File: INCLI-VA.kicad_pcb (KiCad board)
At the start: 2 copper layers, 100 x 100 mm, 168 parts, among them J1 MSTBV 2,5/5-GF-5,08, J2 MSTBV 2,5/2-GF-5,08, J401 USB4105-GF-A, J402 UART0, Q101 STD18NF25, Q102 IPD30N10S3L-34, Q701 DMN10H220LQ, Q751 DMN10H220LQ, SW401 RESET, SW402 BOOT, U101 LM74930QRGERQ1, U201 LMR38010SQDDARQ1, U301 TPS62A02QDRLRQ1, U302 LP5907QMFX-3.3Q1, U401 ESP32-S3-WROOM-1-N8R2, U402 USBLC6-2SC6, U501 SCL3300-D01, U502 ASM330LHHTR, U503 AS5147U-HTSM, U601 ADM3055E, U701 74AHCT1G126, U751 74AHCT1G126, U801 TPS3828-33Q1

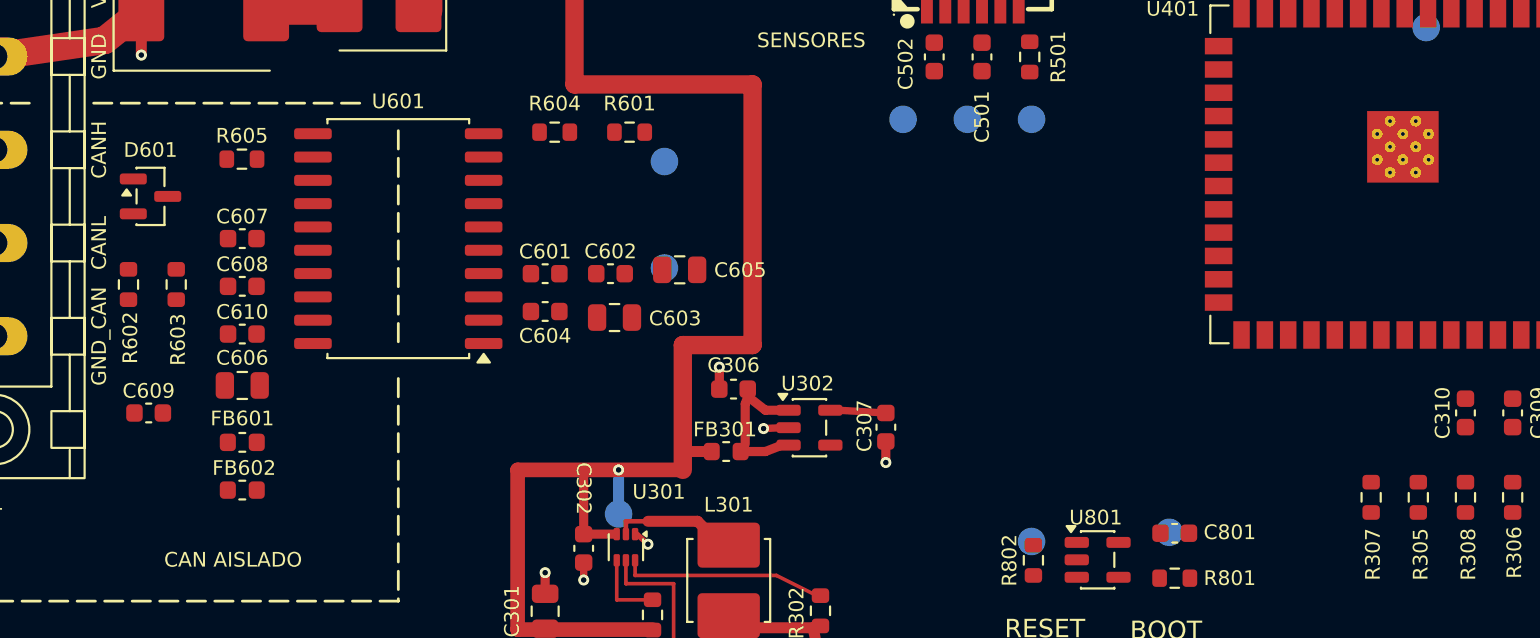
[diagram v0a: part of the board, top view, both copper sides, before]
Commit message: [Codex] ruteo etapa 2 parcial: fuente CAN, desacoples, señales lógicas y TP301
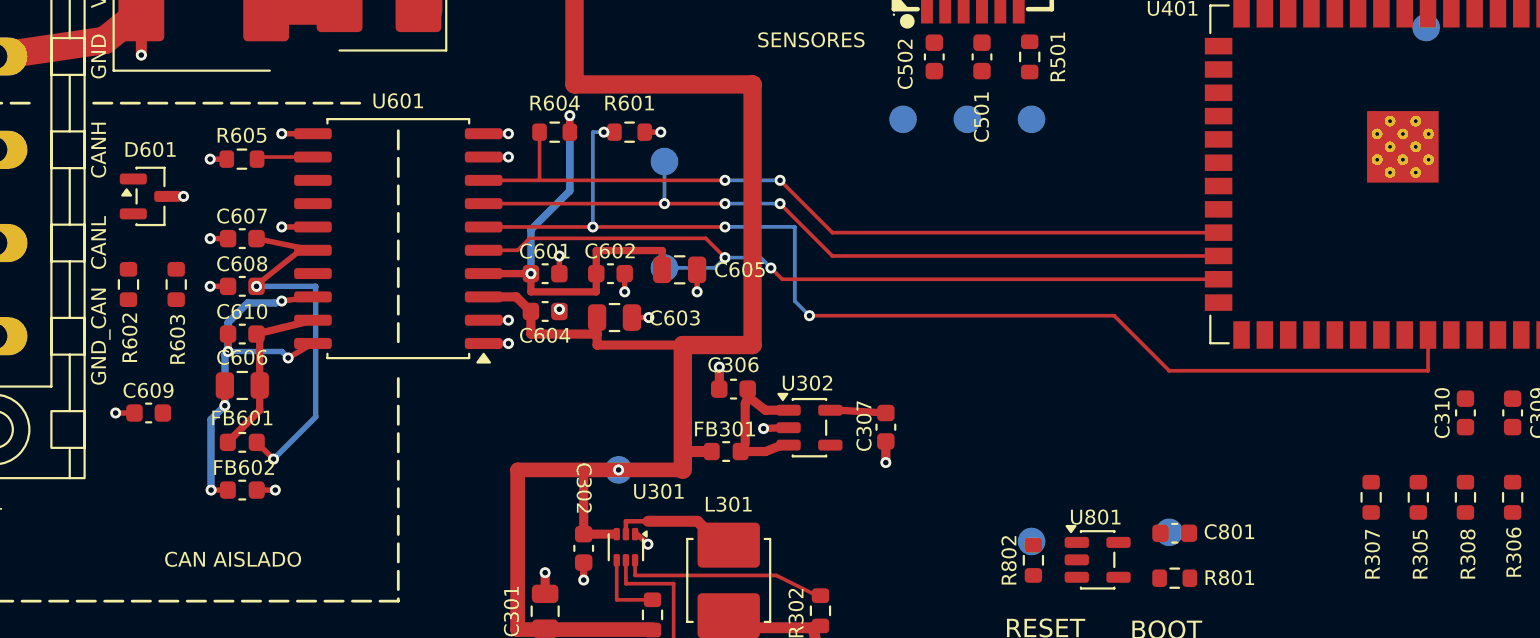
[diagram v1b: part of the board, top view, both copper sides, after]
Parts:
- moved TP301 2.40 mm to (140.0, 131.6)
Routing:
- net /CAN_SILENT: track 0.00 -> 65.3 mm, vias 0 -> 4
- net /CAN_RX: track 0.00 -> 44.8 mm, vias 0 -> 2
- net /CAN_STBY: track 0.00 -> 43.8 mm, vias 0 -> 2
- net /CAN_TX: track 0.00 -> 43.5 mm, vias 0 -> 3
- net +3V3_D: track 15.9 -> 40.3 mm, vias 1 -> 3
- net /60_can/GNDISO_CAN: track 0.00 -> 22.6 mm, vias 0 -> 5
- net /60_can/V_SOIN: track 0.00 -> 21.8 mm, vias 0 -> 2
- net +5V_VEH: track 148.1 -> 159.6 mm
- net GND_VEH: track 40.4 -> 50.8 mm, vias 19 -> 29
- net /60_can/V_SOOUT: track 0.09 -> 9.95 mm
- net GND_CAN: track 0.00 -> 9.15 mm, vias 0 -> 8
- net /60_can/CAN_RS: track 0.16 -> 3.09 mm

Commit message: [Codex] ruteo etapa 2: cierra CAN, terminación y verificación de longitudes
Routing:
- net /BUS_CAN_H: track 0.00 -> 30.8 mm, vias 0 -> 2
- net /BUS_CAN_L: track 0.00 -> 25.0 mm
- net Net-(C609-Pad1): track 0.03 -> 11.6 mm, vias 0 -> 2

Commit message: [Codex] ruteo: audita continuidad CAN y avanza etapa 3 parcial
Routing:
- net +3V3_D: track 40.3 -> 119.0 mm, vias 3 -> 5
- net /MCU_RST_N: track 0.00 -> 62.1 mm, vias 0 -> 2
- net /40_mcu/BOOT: track 0.00 -> 29.2 mm, vias 0 -> 3
- net /40_mcu/U0TXD: track 0.00 -> 24.9 mm, vias 0 -> 2
- net /40_mcu/U0RXD: track 0.00 -> 23.1 mm
- net GND_VEH: track 50.8 -> 58.8 mm, vias 29 -> 36
- net Net-(U801-~{RESET}): track 0.00 -> 4.16 mm

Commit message: [Codex] ruteo etapa 3: agrega C404 y completa avance salvo escape USB
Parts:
- added C404: 100nF, Capacitor_SMD:C_0603_1608Metric, F.Cu at (189.6, 81.5)
- moved R401 52.7 mm to (187.0, 100.1), turned to -90 degrees
- moved C402 0.75 mm to (189.2, 104.0), turned to 90 degrees
- moved C401 0.59 mm to (189.2, 100.6), turned to 90 degrees
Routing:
- net +3V3_D: track 119.0 -> 199.1 mm, vias 5 -> 8
- net /40_mcu/USB_D+: track 0.00 -> 52.7 mm, vias 0 -> 2
- net /40_mcu/USB_D-: track 0.00 -> 52.3 mm, vias 0 -> 2
- net /40_mcu/VBUS: track 0.00 -> 23.0 mm, vias 0 -> 3
- net /40_mcu/CC1: track 0.00 -> 9.94 mm
- net /40_mcu/CC2: track 0.00 -> 8.91 mm
- net GND_VEH: track 58.8 -> 65.2 mm, vias 36 -> 44
- net /MCU_RST_N: track 62.1 -> 66.9 mm

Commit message: [Codex] ruteo etapa 3: cierra USB con estrechamiento autorizado y verificación final
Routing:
- net /40_mcu/USB_D-: track 52.3 -> 54.2 mm
